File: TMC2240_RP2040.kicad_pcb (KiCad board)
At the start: 4 copper layers, 62.8 x 62.8 mm, 119 parts, among them J1 V_{MOTOR}, J10 Screw_Terminal_01x01, J11 Screw_Terminal_01x01, J12 Screw_Terminal_01x01, J14 RSS232Out, J15 RSS232In, J16 SWD, J19 USB_C_Receptacle_USB2.0, J2 LIMIT, J4 Motor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

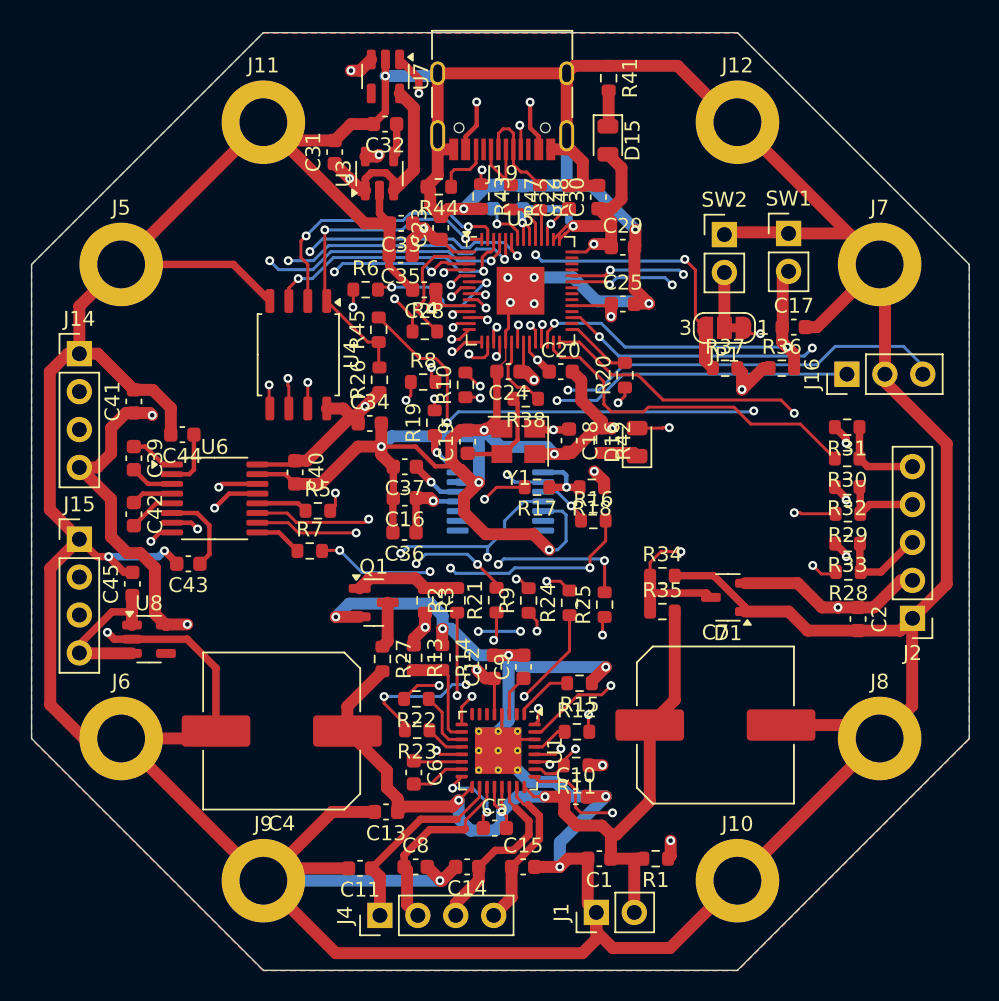
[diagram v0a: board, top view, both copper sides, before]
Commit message: Added an ADC input pin, and protection diodes. Updated the OV load resistor to 0805. Cleaned up a few silk screen overlaps.
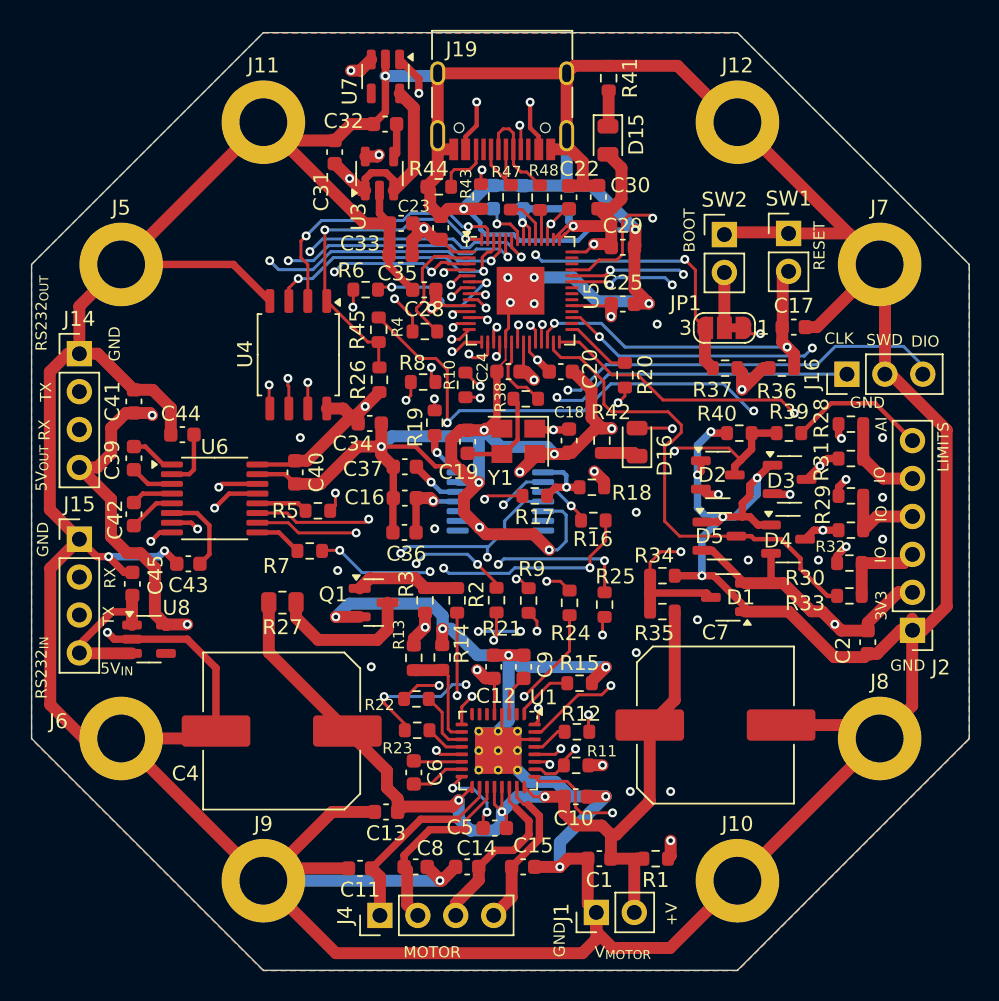
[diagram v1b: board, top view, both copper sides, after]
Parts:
- added D2: 0.1A, Package_TO_SOT_SMD:SOT-23-3, F.Cu at (140.0, 134.1)
- added D3: 0.1A, Package_TO_SOT_SMD:SOT-23-3, F.Cu at (144.8, 134.4)
- added D4: 0.1A, Package_TO_SOT_SMD:SOT-23-3, F.Cu at (144.7, 138.4)
- added D5: 0.1A, Package_TO_SOT_SMD:SOT-23-3, F.Cu at (140.1, 138.2)
- added R39: 100Ω, Resistor_SMD:R_0603_1608Metric, F.Cu at (144.7, 131.3)
- added R40: 100Ω, Resistor_SMD:R_0603_1608Metric, F.Cu at (141.4, 131.3)
- J2: footprint Connector_PinHeader_2.54mm:PinHeader_1x05_P2.54mm_Vertical -> Connector_PinHeader_2.54mm:PinHeader_1x06_P2.54mm_Vertical
- R27: footprint Resistor_SMD:R_0603_1608Metric -> Resistor_SMD:R_0805_2012Metric
- moved R28 9.90 mm to (148.9, 130.7)
- moved R27 7.69 mm to (110.8, 142.7), turned to 180 degrees
- moved R30 7.00 mm to (148.8, 140.0)
- moved R33 3.50 mm to (148.8, 142.2)
- moved R32 2.91 mm to (148.9, 137.8)
- moved R31 2.11 mm to (148.9, 133.0)
- moved C2 1.68 mm to (150.0, 145.3)
- moved R29 1.22 mm to (148.9, 135.5)
- moved J2 0.80 mm to (153.0, 144.5)
- moved R17 0.59 mm to (127.7, 135.5)
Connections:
- R28 pad 1: Net-(J2-Pin_3) -> Net-(J2-Pin_5)
- R28 pad 2: /RP2040uC/SDA0_GP20 -> +3.3V
- R29 pad 2: /RP2040uC/RX0_SCL0_SPIS0_GP17 -> +3.3V
- R30 pad 1: Net-(J2-Pin_5) -> Net-(J2-Pin_3)
- R30 pad 2: /RP2040uC/TX0_SDA0_SPIO0_GP16 -> +3.3V
- R31 pad 2: +3.3V -> /AccessoryConnections/LIMITL
- R32 pad 2: +3.3V -> /AccessoryConnections/LIMITM
- R33 pad 2: +3.3V -> /AccessoryConnections/LIMITH
- U5 pad 27: /RP2040uC/TX0_SDA0_SPIO0_GP16 -> /AccessoryConnections/LIMITH
- U5 pad 28: /RP2040uC/RX0_SCL0_SPIS0_GP17 -> /AccessoryConnections/LIMITM
- U5 pad 31: /RP2040uC/SDA0_GP20 -> /AccessoryConnections/LIMITL
- U5 pad 39: /RP2040uC/ADC1_GP27 -> /AccessoryConnections/ADC
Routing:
- net GND: track 555.0 -> 591.6 mm, vias 24 -> 46
- net /AccessoryConnections/ADC: track 0.00 -> 34.5 mm, vias 0 -> 2
- net /RP2040uC/SDA0_GP20: track 33.8 -> 0.00 mm, vias 3 -> 0
- net /AccessoryConnections/LIMITH: track 0.00 -> 33.1 mm
- net /AccessoryConnections/LIMITM: track 0.00 -> 28.8 mm, vias 0 -> 2
- net /AccessoryConnections/LIMITL: track 0.00 -> 28.2 mm, vias 0 -> 3
- net /RP2040uC/RX0_SCL0_SPIS0_GP17: track 27.2 -> 0.00 mm, vias 2 -> 0
- net /RP2040uC/TX0_SDA0_SPIO0_GP16: track 23.5 -> 0.00 mm
- net +3.3V: track 233.6 -> 252.3 mm, vias 19 -> 21
- net Net-(J2-Pin_6): track 0.00 -> 9.31 mm
- net Net-(Q1-D): track 3.09 -> 9.86 mm
- net VCC: track 63.1 -> 68.9 mm
- net /RP2040uC/~{USB_BOOT}: track 37.1 -> 38.6 mm
- net /RP2040uC/RX1_SCL0_SPIS0_GP5: track 30.0 -> 28.7 mm
- net /AS5048AEncoder/CLK: track 31.2 -> 32.3 mm
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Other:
- board text added: "+V"
- board text added: "3V3"
- board text added: "5V_{IN}"
- board text added: "5V_{OUT}"
- board text added: "AI"
- board text added: "BOOT"
- board text added: "CLK"
- board text added: "DIO"
- board text added: "GND"
- board text added: "IO"
- board text added: "LIMITS"
- board text added: "MOTOR"
- board text added: "RESET"
- board text added: "RS232_{IN}"
- board text added: "RS232_{OUT}"
- board text added: "RX"
- board text added: "SWD"
- board text added: "TX"
- board text added: "V_{MOTOR}"

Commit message: Added more silk screen labels and generated manufacturing files.
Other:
- board text added: "RP2040 Stepper Controller V1.0 TMC2240 stepper driver MAX3232 RS232 in/out AS5048 encoder"
